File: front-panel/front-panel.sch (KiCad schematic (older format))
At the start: 12 parts, among them P2 LCD, SW1 LEFT, SW2 UP, SW3 DOWN, SW4 RIGHT, SW5 ENTER

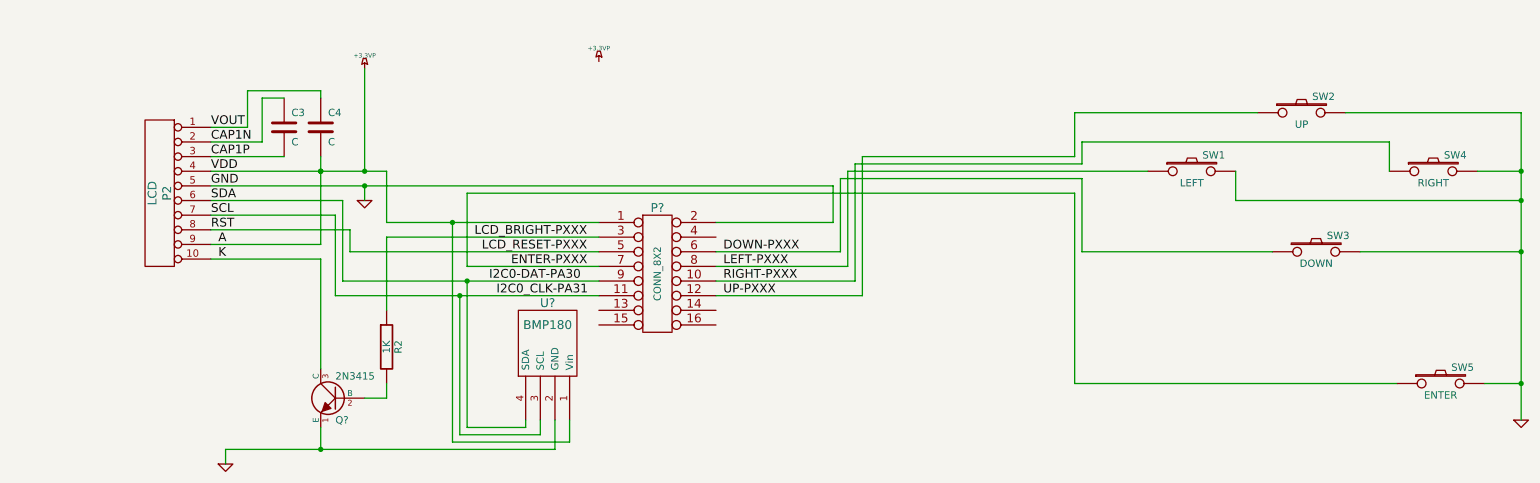
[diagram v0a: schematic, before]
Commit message: Fix connector and power labels
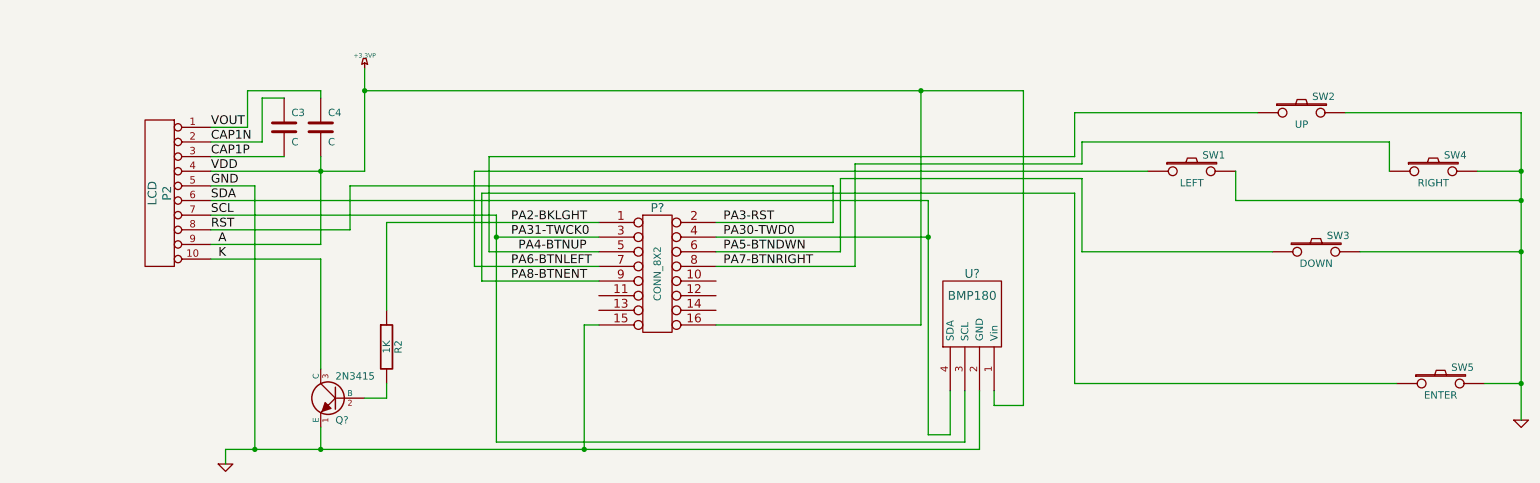
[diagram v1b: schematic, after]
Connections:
- net +3.3VP: now also P?.16; no longer P?.1
- net GND: now also P?.15; no longer P?.2
- net PA30-TWD0: now reaches P?.4
- net PA30-TWD0: now also P2.6 (P6), U?.4 (SDA)
- net DOWN-PXXX renamed PA5-BTNDWN
- net ENTER-PXXX renamed PA6-BTNLEFT
- net PA6-BTNLEFT: now also SW1.1; no longer SW5.1
- removed net I2C0-DAT-PA30: P2.6 (P6), P?.9, U?.4 (SDA)
- net I2C0_CLK-PA31 renamed PA31-TWCK0
- net PA31-TWCK0: now also P?.3; no longer P?.11
- net LCD_BRIGHT-PXXX renamed PA2-BKLGHT
- net PA2-BKLGHT: now also P?.1; no longer P?.3
- net LCD_RESET-PXXX renamed PA3-RST
- net PA3-RST: now also P?.2; no longer P?.5
- net LEFT-PXXX renamed PA7-BTNRIGHT
- net PA7-BTNRIGHT: now also SW4.1; no longer SW1.1
- net RIGHT-PXXX: no longer names the net of P?.10
- net RIGHT-PXXX: no longer SW4.1
- net UP-PXXX: no longer names the net of P?.12
- net UP-PXXX: no longer SW2.1
- new net PA4-BTNUP: P?.5, SW2.1
- new net PA8-BTNENT: P?.9, SW5.1
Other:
- moved on the sheet: U?
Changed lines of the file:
@@
 LIBS:valves
 LIBS:MyKicadLib
+LIBS:front-panel-cache
 EELAYER 27 0
 EELAYER END
@@
 Sheet 1 1
 Title ""
-Date "4 may 2015"
+Date "1 jan 2016"
 Rev ""
 Comp ""
@@
 Comment4 ""
 $EndDescr
-Connection ~ 3600 1950
-Wire Wire Line
-	3600 1950 3600 3450
-Wire Wire Line
-	3600 3450 4400 3450
-Wire Wire Line
-	4400 3450 4400 3300
-Connection ~ 3000 1600
-Wire Wire Line
-	1950 1600 3150 1600
-Wire Wire Line
-	3150 1600 3150 1950
-Wire Wire Line
-	3150 1950 4600 1950
-Connection ~ 2700 3500
-Wire Wire Line
-	4300 3500 2050 3500
-Wire Wire Line
-	4300 3500 4300 3300
-Connection ~ 3700 2350
-Wire Wire Line
-	3700 2350 3700 3350
-Wire Wire Line
-	3700 3350 4100 3350
-Wire Wire Line
-	4100 3350 4100 3300
+Wire Wire Line
+	3000 1600 1950 1600
+Wire Wire Line
+	2050 3500 7200 3500
 Wire Wire Line
 	3000 3150 3150 3150
@@
 	3150 3150 3150 3050
 Wire Wire Line
-	6400 2450 6400 1500
-Wire Wire Line
-	6400 2450 5400 2450
-Wire Wire Line
-	6300 2250 6300 1600
-Wire Wire Line
-	6300 2250 5400 2250
-Wire Wire Line
-	3700 2250 3700 1750
-Wire Wire Line
-	3700 2250 4600 2250
-Wire Wire Line
 	10050 3050 7850 3050
 Wire Wire Line
 	7850 3050 7850 1750
 Wire Wire Line
-	7850 1750 3700 1750
-Wire Wire Line
-	6300 1600 8350 1600
+	7850 1750 3800 1750
+Wire Wire Line
+	3750 1600 8350 1600
 Wire Wire Line
 	9100 1200 7850 1200
@@
 	7850 1200 7850 1500
 Wire Wire Line
-	7850 1500 6400 1500
+	7850 1500 3850 1500
 Connection ~ 10900 2150
 Wire Wire Line
@@
 	8950 1800 8950 1600
 Wire Wire Line
-	4600 2150 2900 2150
-Wire Wire Line
-	2900 2150 2900 2000
+	2900 1700 2900 2000
 Wire Wire Line
 	2900 2000 1950 2000
 Wire Wire Line
-	2800 1900 2800 2450
-Wire Wire Line
-	2800 1900 1950 1900
-Wire Wire Line
-	4600 2350 2850 2350
-Wire Wire Line
-	2850 2350 2850 1800
-Wire Wire Line
-	2850 1800 1950 1800
+	1950 1900 3900 1900
+Wire Wire Line
+	1950 1800 6850 1800
 Connection ~ 2700 1600
 Wire Wire Line
@@
 Wire Wire Line
 	2700 1050 2700 1100
-Wire Wire Line
-	3000 1700 3000 1800
 Wire Wire Line
 	9700 1200 10900 1200
@@
 	7900 1650 6250 1650
 Wire Wire Line
-	2800 2450 4600 2450
-Wire Wire Line
 	5400 2150 6250 2150
 Wire Wire Line
 	6250 2150 6250 1650
 Wire Wire Line
-	5400 2350 6350 2350
-Wire Wire Line
-	6350 2350 6350 1550
+	6350 1550 6350 2250
 Wire Wire Line
 	2050 3500 2050 3600
 Wire Wire Line
 	2700 2100 1950 2100
-Connection ~ 2700 1600
-Wire Wire Line
-	2700 3350 2700 3500
-Wire Wire Line
-	4600 2050 3150 2050
-Wire Wire Line
-	3150 2050 3150 2550
+Wire Wire Line
+	2700 3500 2700 3350
 Wire Wire Line
 	1950 2200 2700 2200
@@
 	2700 2200 2700 2950
 Wire Wire Line
-	4200 3300 4200 3400
-Wire Wire Line
-	4200 3400 3650 3400
-Wire Wire Line
-	3650 3400 3650 2450
-Connection ~ 3650 2450
-Wire Wire Line
-	5400 1950 6200 1950
-Wire Wire Line
-	6200 1950 6200 1700
-Wire Wire Line
-	6200 1700 1950 1700
-Connection ~ 3000 1700
+	2250 1700 1950 1700
 $Comp
 L CONN_8X2 P?
@@
 L BMP180 U?
 U 1 1 553D211F
-P 4250 2750
-F 0 "U?" H 4250 3000 60  0000 C CNN
-F 1 "BMP180" H 4250 2850 60  0000 C CNN
-F 2 "" H 4250 2750 60  0001 C CNN
-F 3 "" H 4250 2750 60  0001 C CNN
-	1    4250 2750
+P 7150 2550
+F 0 "U?" H 7150 2800 60  0000 C CNN
+F 1 "BMP180" H 7150 2650 60  0000 C CNN
+F 2 "" H 7150 2550 60  0001 C CNN
+F 3 "" H 7150 2550 60  0001 C CNN
+	1    7150 2550
 	1    0    0    -1
 $EndComp
@@
 	-1   0    0    -1
 $EndComp
-Text Label 3900 2450 0    60   ~ 0
-I2C0_CLK-PA31
-Text Label 3850 2350 0    60   ~ 0
-I2C0-DAT-PA30
-Text Label 4000 2250 0    60   ~ 0
-ENTER-PXXX
-Text Label 3800 2150 0    60   ~ 0
-LCD_RESET-PXXX
-Text Label 3750 2050 0    60   ~ 0
-LCD_BRIGHT-PXXX
-Text Label 5450 2450 0    60   ~ 0
-UP-PXXX
-Text Label 5450 2350 0    60   ~ 0
-RIGHT-PXXX
-Text Label 5450 2250 0    60   ~ 0
-LEFT-PXXX
 Text Label 5450 2150 0    60   ~ 0
-DOWN-PXXX
+PA5-BTNDWN
 $Comp
 L R R2
@@
 A
 $Comp
-L +3.3VP #PWR03
-U 1 1 55336CF9
-P 4600 850
-F 0 "#PWR03" H 4650 880 20  0001 C CNN
-F 1 "+3.3VP" H 4600 940 30  0000 C CNN
-F 2 "" H 4600 850 60  0001 C CNN
-F 3 "" H 4600 850 60  0001 C CNN
-	1    4600 850
-	1    0    0    -1
-$EndComp
-$Comp
 L GND #PWR04
 U 1 1 55336A39
@@
 Text Label 1950 1700 0    60   ~ 0
 GND
-$Comp
-L GND #PWR06
-U 1 1 553365FD
-P 3000 1800
-F 0 "#PWR06" H 3000 1800 30  0001 C CNN
-F 1 "GND" H 3000 1730 30  0001 C CNN
-F 2 "" H 3000 1800 60  0001 C CNN
-F 3 "" H 3000 1800 60  0001 C CNN
-	1    3000 1800
-	1    0    0    -1
-$EndComp
 $Comp
 L +3.3VP #PWR07
@@
 	-1   0    0    -1
 $EndComp
+Wire Wire Line
+	5400 2650 6800 2650
+Wire Wire Line
+	6800 2650 6800 1050
+Wire Wire Line
+	3000 1050 7500 1050
+Connection ~ 3000 1050
+Wire Wire Line
+	7300 3100 7300 3200
+Wire Wire Line
+	7300 3200 7500 3200
+Wire Wire Line
+	7500 3200 7500 1050
+Connection ~ 6800 1050
+Wire Wire Line
+	7200 3500 7200 3100
+Connection ~ 2700 3500
+Wire Wire Line
+	4600 2650 4500 2650
+Wire Wire Line
+	4500 2650 4500 3500
+Connection ~ 4500 3500
+Wire Wire Line
+	2250 1700 2250 3500
+Connection ~ 2250 3500
+Wire Wire Line
+	4600 1950 3150 1950
+Wire Wire Line
+	3150 1950 3150 2550
+Text Label 4000 1950 0    60   ~ 0
+PA2-BKLGHT
+Wire Wire Line
+	5400 1950 6200 1950
+Wire Wire Line
+	6200 1950 6200 1700
+Wire Wire Line
+	6200 1700 2900 1700
+Text Label 5450 1950 0    60   ~ 0
+PA3-RST
+Text Label 4000 2050 0    60   ~ 0
+PA31-TWCK0
+Wire Wire Line
+	4600 2050 3900 2050
+Wire Wire Line
+	3900 1900 3900 3450
+Wire Wire Line
+	3900 3450 7100 3450
+Wire Wire Line
+	7100 3450 7100 3100
+Connection ~ 3900 2050
+Wire Wire Line
+	5400 2050 6850 2050
+Wire Wire Line
+	6850 1800 6850 3400
+Wire Wire Line
+	6850 3400 7000 3400
+Wire Wire Line
+	7000 3400 7000 3100
+Text Label 5450 2050 0    60   ~ 0
+PA30-TWD0
+Connection ~ 6850 2050
+Wire Wire Line
+	3850 1500 3850 2150
+Wire Wire Line
+	3850 2150 4600 2150
+Text Label 4050 2150 0    60   ~ 0
+PA4-BTNUP
+Wire Wire Line
+	6350 2250 5400 2250
+Text Label 5450 2250 0    60   ~ 0
+PA7-BTNRIGHT
+Wire Wire Line
+	4600 2350 3800 2350
+Wire Wire Line
+	3800 2350 3800 1750
+Text Label 4000 2350 0    60   ~ 0
+PA8-BTNENT
+Wire Wire Line
+	3750 1600 3750 2250
+Wire Wire Line
+	3750 2250 4600 2250
+Text Label 4000 2250 0    60   ~ 0
+PA6-BTNLEFT
 $EndSCHEMATC

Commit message: Power revision and add ina219 sensor
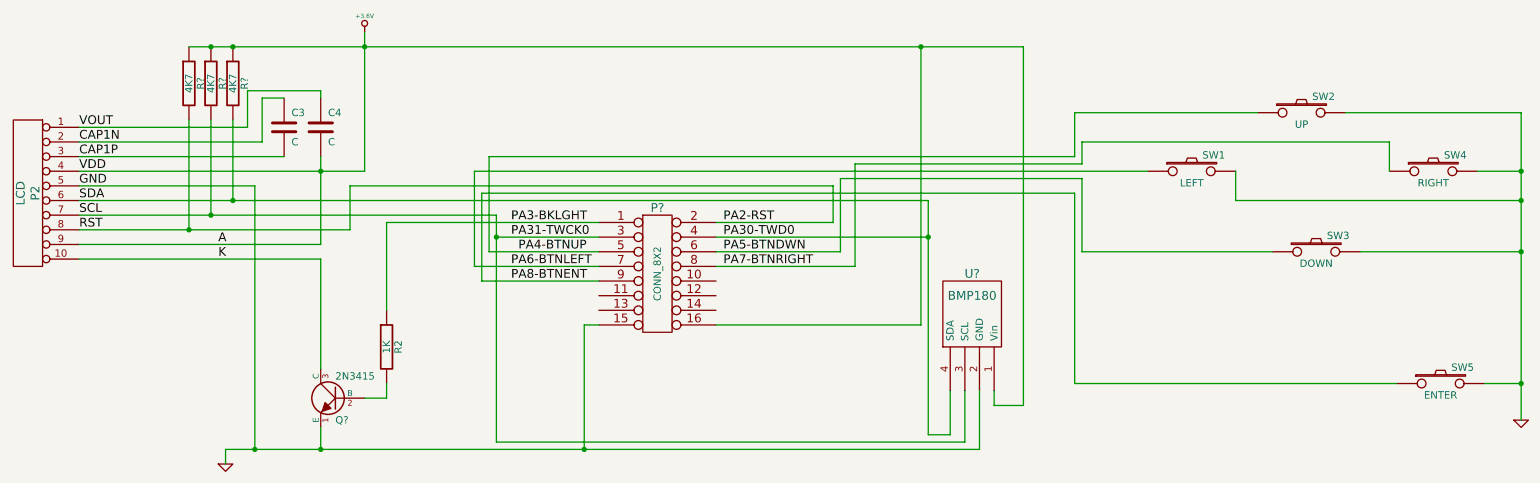
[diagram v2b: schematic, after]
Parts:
- added R? (x3): 4K7, symbol R
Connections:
- net PA30-TWD0: now also R?.2
- net PA31-TWCK0: now also R?.2
- net +3.3VP renamed +3.6V
- net +3.6V: now also R?.1, R?.1, R?.1
- net PA2-BKLGHT renamed PA3-BKLGHT
- net PA3-RST renamed PA2-RST
- net PA2-RST: now also R?.2
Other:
- moved on the sheet: P2
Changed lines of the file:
@@
 Sheet 1 1
 Title ""
-Date "1 jan 2016"
+Date "25 apr 2017"
 Rev ""
 Comp ""
@@
 $EndDescr
 Wire Wire Line
-	3000 1600 1950 1600
+	3000 1600 1050 1600
 Wire Wire Line
 	2050 3500 7200 3500
@@
 	8950 1800 8950 1600
 Wire Wire Line
-	2900 1700 2900 2000
-Wire Wire Line
-	2900 2000 1950 2000
-Wire Wire Line
-	1950 1900 3900 1900
-Wire Wire Line
-	1950 1800 6850 1800
+	2900 2000 2900 1700
+Wire Wire Line
+	1050 2000 2900 2000
+Wire Wire Line
+	1050 1900 3900 1900
+Wire Wire Line
+	1050 1800 6850 1800
 Connection ~ 2700 1600
 Wire Wire Line
-	3000 900  3000 1600
-Wire Wire Line
-	2200 1050 2700 1050
-Wire Wire Line
-	2200 1050 2200 1300
-Wire Wire Line
-	2200 1300 1950 1300
-Wire Wire Line
-	1950 1500 2450 1500
+	3000 650  3000 1600
+Wire Wire Line
+	1050 1500 2450 1500
 Wire Wire Line
 	2700 1500 2700 2100
 Wire Wire Line
-	1950 1400 2300 1400
+	1050 1400 2300 1400
 Wire Wire Line
 	2300 1400 2300 1100
 Wire Wire Line
 	2300 1100 2450 1100
-Wire Wire Line
-	2700 1050 2700 1100
 Wire Wire Line
 	9700 1200 10900 1200
@@
 	2050 3500 2050 3600
 Wire Wire Line
-	2700 2100 1950 2100
+	2700 2100 1050 2100
 Wire Wire Line
 	2700 3500 2700 3350
 Wire Wire Line
-	1950 2200 2700 2200
+	1050 2200 2700 2200
 Wire Wire Line
 	2700 2200 2700 2950
 Wire Wire Line
-	2250 1700 1950 1700
+	2250 1700 1050 1700
 $Comp
 L CONN_8X2 P?
@@
 	1    0    0    -1
 $EndComp
-Text Label 1950 2000 0    60   ~ 0
+Text Label 1050 2000 0    60   ~ 0
 RST
 $Comp
@@
 	1    0    0    -1
 $EndComp
-Text Label 1950 1900 0    60   ~ 0
+Text Label 1050 1900 0    60   ~ 0
 SCL
-Text Label 1950 1800 0    60   ~ 0
+Text Label 1050 1800 0    60   ~ 0
 SDA
-Text Label 1950 1700 0    60   ~ 0
+Text Label 1050 1700 0    60   ~ 0
 GND
-$Comp
-L +3.3VP #PWR07
-U 1 1 553365BE
-P 3000 900
-F 0 "#PWR07" H 3050 930 20  0001 C CNN
-F 1 "+3.3VP" H 3000 990 30  0000 C CNN
-F 2 "" H 3000 900 60  0001 C CNN
-F 3 "" H 3000 900 60  0001 C CNN
-	1    3000 900
-	1    0    0    -1
-$EndComp
 $Comp
 L C C4
@@
 	1    0    0    -1
 $EndComp
-Text Label 1950 1400 0    60   ~ 0
+Text Label 1050 1400 0    60   ~ 0
 CAP1N
-Text Label 1950 1500 0    60   ~ 0
+Text Label 1050 1500 0    60   ~ 0
 CAP1P
-Text Label 1950 1300 0    60   ~ 0
-VOUT
-Text Label 1950 1600 0    60   ~ 0
+Text Label 1050 1600 0    60   ~ 0
 VDD
 $Comp
@@
 L CONN_10 P2
 U 1 1 55336217
-P 1600 1750
-F 0 "P2" V 1550 1750 60  0000 C CNN
-F 1 "LCD" V 1650 1750 60  0000 C CNN
-F 2 "" H 1600 1750 60  0001 C CNN
-F 3 "" H 1600 1750 60  0001 C CNN
-	1    1600 1750
+P 700 1750
+F 0 "P2" V 650 1750 60  0000 C CNN
+F 1 "LCD" V 750 1750 60  0000 C CNN
+F 2 "" H 700 1750 60  0001 C CNN
+F 3 "" H 700 1750 60  0001 C CNN
+	1    700  1750
 	-1   0    0    -1
 $EndComp
@@
 	5400 2650 6800 2650
 Wire Wire Line
-	6800 2650 6800 1050
-Wire Wire Line
-	3000 1050 7500 1050
-Connection ~ 3000 1050
+	6800 2650 6800 750
+Wire Wire Line
+	1800 750  7500 750
+Connection ~ 3000 750
 Wire Wire Line
 	7300 3100 7300 3200
@@
 	7300 3200 7500 3200
 Wire Wire Line
-	7500 3200 7500 1050
-Connection ~ 6800 1050
+	7500 3200 7500 750
+Connection ~ 6800 750
 Wire Wire Line
 	7200 3500 7200 3100
@@
 	3150 1950 3150 2550
 Text Label 4000 1950 0    60   ~ 0
-PA2-BKLGHT
+PA3-BKLGHT
 Wire Wire Line
 	5400 1950 6200 1950
@@
 	6200 1700 2900 1700
 Text Label 5450 1950 0    60   ~ 0
-PA3-RST
+PA2-RST
 Text Label 4000 2050 0    60   ~ 0
 PA31-TWCK0
@@
 Text Label 4000 2250 0    60   ~ 0
 PA6-BTNLEFT
+$Comp
+L R R?
+U 1 1 58FA50A2
+P 2100 1000
+F 0 "R?" V 2180 1000 50  0000 C CNN
+F 1 "4K7" V 2100 1000 50  0000 C CNN
+F 2 "" H 2100 1000 60  0001 C CNN
+F 3 "" H 2100 1000 60  0001 C CNN
+	1    2100 1000
+	1    0    0    -1
+$EndComp
+$Comp
+L R R?
+U 1 1 58FA50B2
+P 1950 1000
+F 0 "R?" V 2030 1000 50  0000 C CNN
+F 1 "4K7" V 1950 1000 50  0000 C CNN
+F 2 "" H 1950 1000 60  0001 C CNN
+F 3 "" H 1950 1000 60  0001 C CNN
+	1    1950 1000
+	1    0    0    -1
+$EndComp
+$Comp
+L R R?
+U 1 1 58FA50B8
+P 1800 1000
+F 0 "R?" V 1880 1000 50  0000 C CNN
+F 1 "4K7" V 1800 1000 50  0000 C CNN
+F 2 "" H 1800 1000 60  0001 C CNN
+F 3 "" H 1800 1000 60  0001 C CNN
+	1    1800 1000
+	1    0    0    -1
+$EndComp
+Connection ~ 1950 750
+Connection ~ 2100 750
+$Comp
+L +3.6V #PWR?
+U 1 1 58FF153A
+P 3000 650
+F 0 "#PWR?" H 3000 610 30  0001 C CNN
+F 1 "+3.6V" H 3000 760 30  0000 C CNN
+F 2 "~" H 3000 650 60  0000 C CNN
+F 3 "~" H 3000 650 60  0000 C CNN
+	1    3000 650
+	1    0    0    -1
+$EndComp
+Wire Wire Line
+	1800 1250 1800 2000
+Connection ~ 1800 2000
+Wire Wire Line
+	1950 1250 1950 1900
+Connection ~ 1950 1900
+Text Label 1050 1300 0    60   ~ 0
+VOUT
+Wire Wire Line
+	2700 1050 2700 1100
+Wire Wire Line
+	2200 1050 2700 1050
+Wire Wire Line
+	2200 1300 2200 1050
+Wire Wire Line
+	1050 1300 2200 1300
+Wire Wire Line
+	2100 1250 2100 1800
+Connection ~ 2100 1800
 $EndSCHEMATC
